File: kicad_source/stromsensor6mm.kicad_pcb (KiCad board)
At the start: 2 copper layers, 47 x 31 mm, 19 parts, among them CN1 SM04B-SRSS-TB, CN10 CONN_01X01, CN11 CONN_01X01, CN2 SM04B-SRSS-TB, CN20 CONN_01X01, CN21 CONN_01X01, CN3 CONN_01X01, U1 INA226

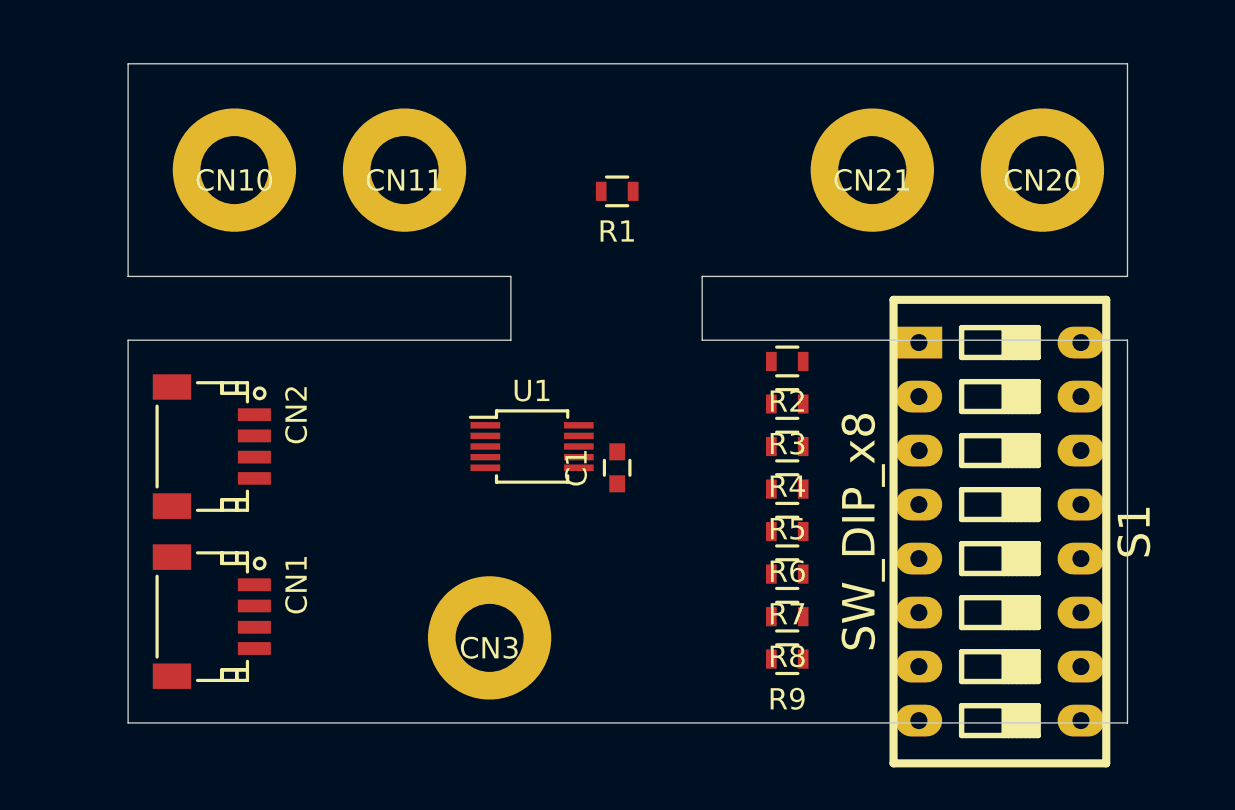
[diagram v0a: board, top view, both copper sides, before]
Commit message: changed mounting holes for connection to wires
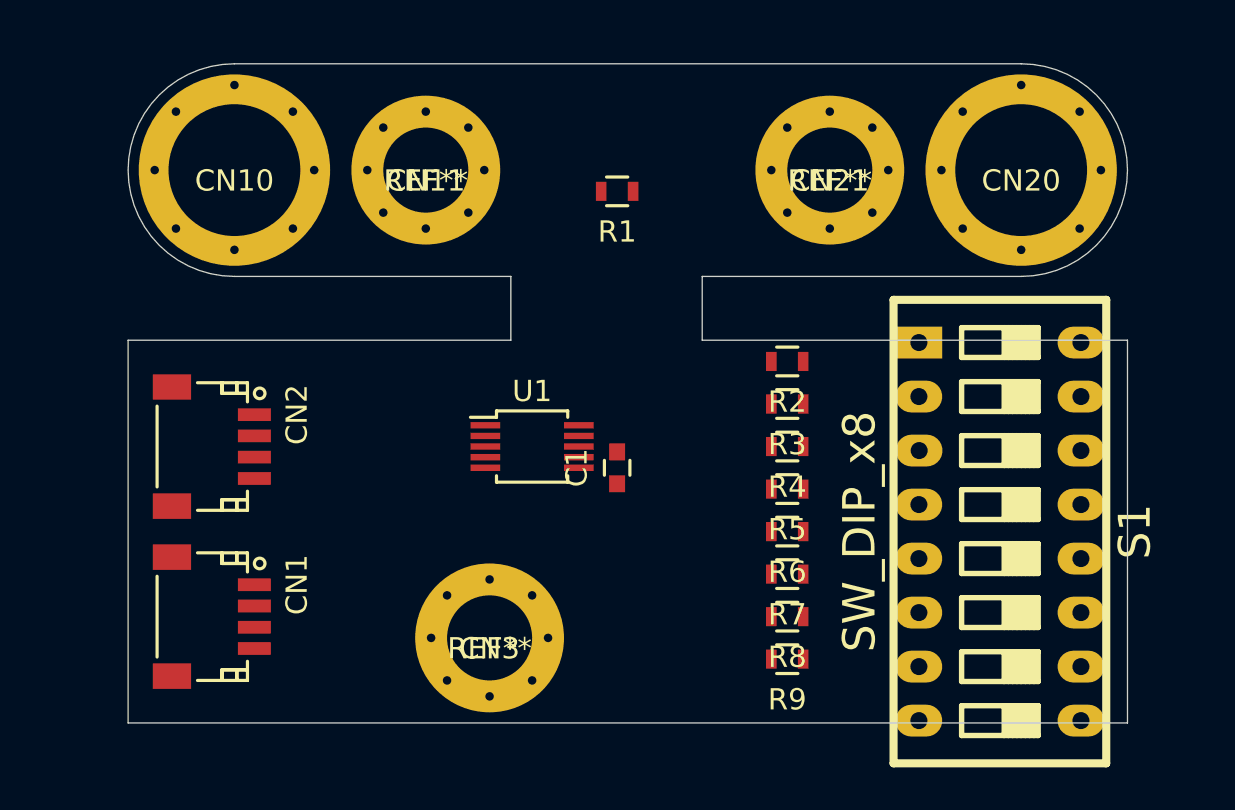
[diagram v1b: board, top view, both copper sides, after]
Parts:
- CN10, CN20: footprint MECH_mounting_holes:MHP_3.2_5.8 -> MECH_mounting_holes:MHP_6.2_9.0
- CN11, CN21, CN3: footprint MECH_mounting_holes:MHP_3.2_5.8 -> MECH_mounting_holes:MHP_4.0_7.0
- moved CN21 2.00 mm to (126.0, 96.0)
- moved CN11 1.00 mm to (107.0, 96.0)
- moved CN20 1.00 mm to (135.0, 96.0)
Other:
- outline, holes or cut-outs redrawn

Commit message: changed current sensor to more robust part
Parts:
- removed R1: 5 mOhm, resistors:R_0603
- added R10: BR3FB5L00, resistors:BR3, F.Cu at (116.0, 97.5)
- added R20: BR3FB5L00, resistors:BR3, F.Cu at (116.0, 94.5)
- moved CN10 4.00 mm to (94.0, 96.0)
- moved CN11 4.00 mm to (103.0, 96.0)
- moved CN20 3.00 mm to (138.0, 96.0)
- moved CN21 3.00 mm to (129.0, 96.0)
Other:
- board size 47 x 31 mm -> 54 x 31 mm

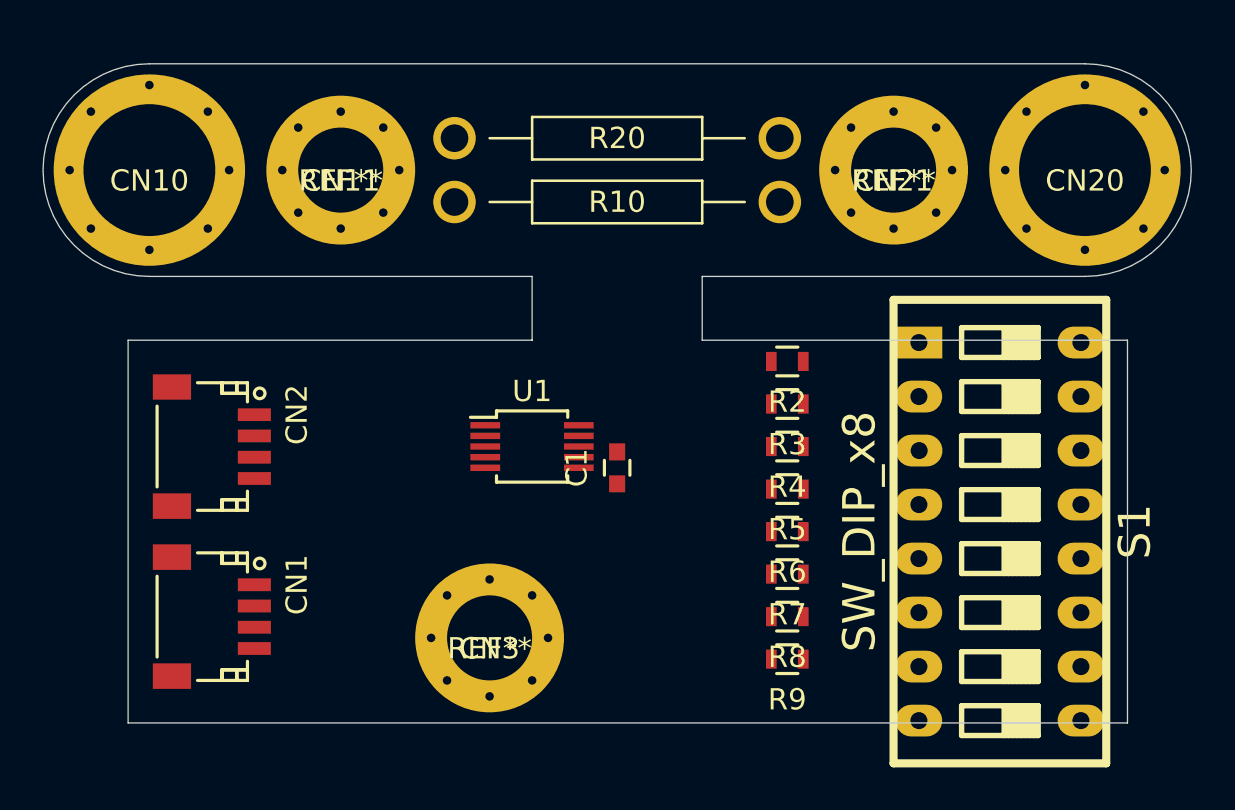
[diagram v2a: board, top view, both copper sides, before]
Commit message: changed dip switch, updated placement and pcb shape
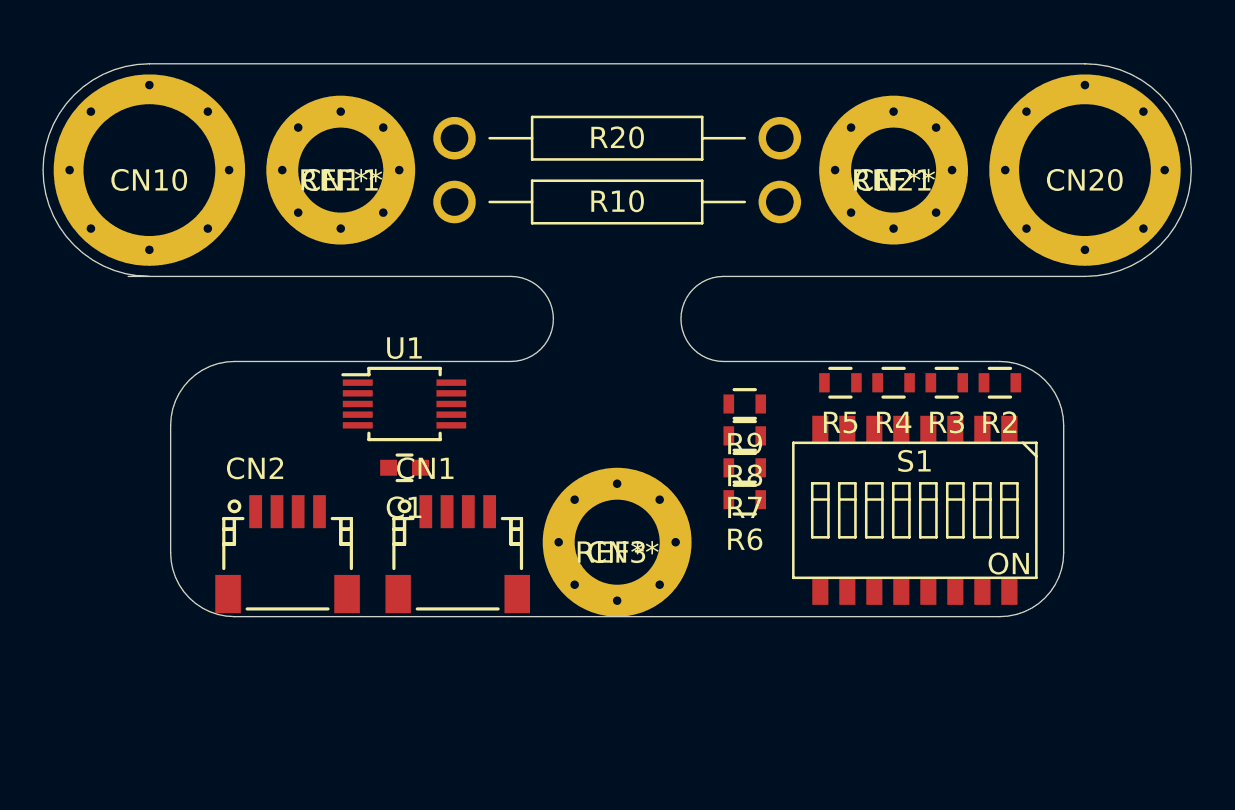
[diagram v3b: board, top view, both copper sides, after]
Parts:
- S1: footprint mechanical-switches:dip_8-300 -> mechanical-switches:WE_416131160808
- moved R9 12.2 mm to (122.0, 107.0)
- moved CN1 11.9 mm to (108.5, 114.0), turned to 0 degrees
- moved R2 10.0 mm to (134.0, 106.0)
- moved C1 10.0 mm to (106.0, 110.0), turned to 180 degrees
- moved R8 8.73 mm to (122.0, 108.5)
- moved R3 7.57 mm to (131.5, 106.0)
- moved CN3 7.50 mm to (116.0, 113.5)
- moved U1 6.32 mm to (106.0, 107.0)
- moved CN2 6.10 mm to (100.5, 114.0), turned to 0 degrees
- moved R4 5.83 mm to (129.0, 106.0)
- moved R5 5.59 mm to (126.5, 106.0)
- moved R7 5.39 mm to (122.0, 110.0)
- moved S1 4.12 mm to (130.0, 112.0), turned to 180 degrees
- moved R6 2.50 mm to (122.0, 111.5)
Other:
- board size 54 x 31 mm -> 54 x 26 mm

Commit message: updated layout, added decoupling capacitor on current sense
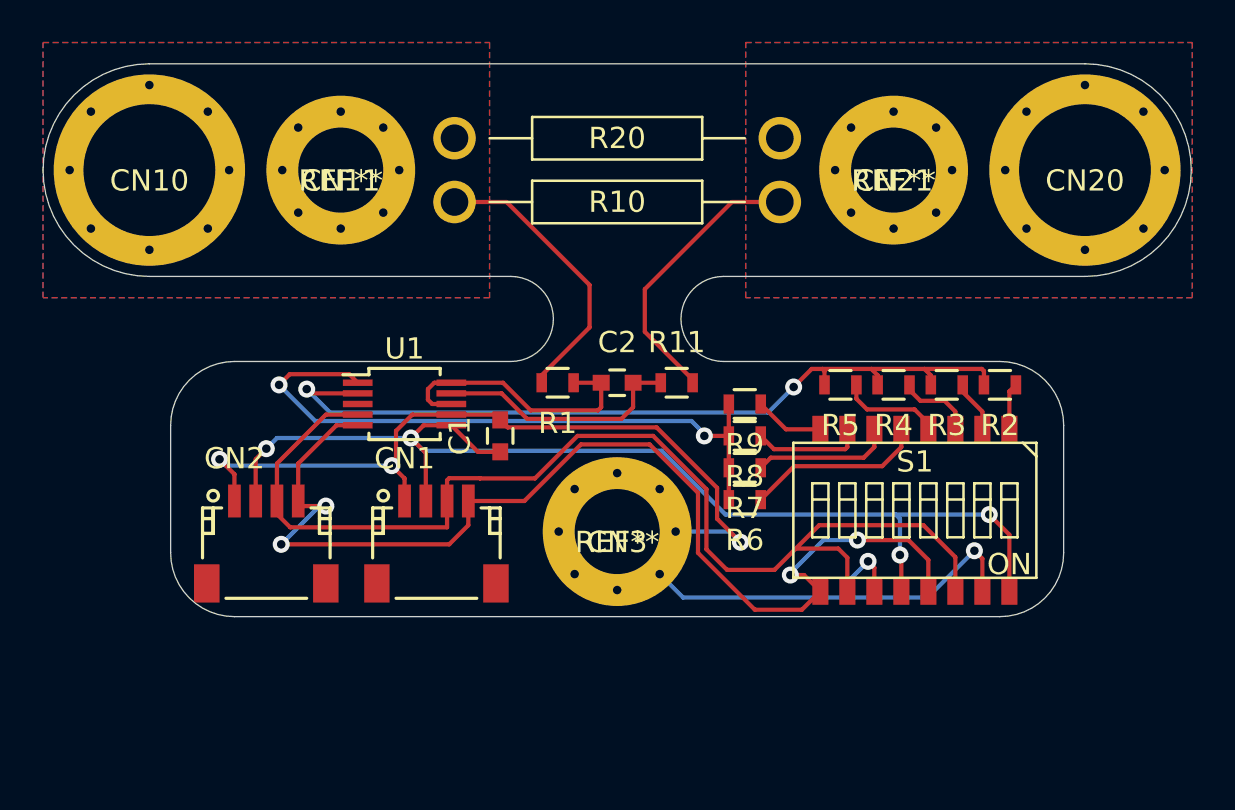
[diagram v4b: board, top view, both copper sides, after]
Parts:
- added C2: 100 nF, capacitors:C_0603, F.Cu at (116.0, 106.0)
- added R1: 100, resistors:R_0603, F.Cu at (113.2, 106.0)
- added R11: 100, resistors:R_0603, F.Cu at (118.8, 106.0)
- moved C1 4.74 mm to (110.5, 108.5), turned to 90 degrees
- moved CN1 1.12 mm to (107.5, 113.5)
- moved CN2 1.12 mm to (99.5, 113.5)
- moved CN3 0.50 mm to (116.0, 113.0)
- moved R2 0.10 mm to (134.0, 106.1)
- moved R3 0.10 mm to (131.5, 106.1)
- moved R4 0.10 mm to (129.0, 106.1)
- moved R5 0.10 mm to (126.5, 106.1)
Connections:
- U1 pad 10: Net-(CN10-Pad1) -> Net-(C2-Pad1)
- U1 pad 8: Net-(CN10-Pad1) -> Net-(C2-Pad1)
- U1 pad 9: Net-(CN20-Pad1) -> Net-(C2-Pad2)
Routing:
- net GND: track 0.00 -> 61.8 mm, vias 0 -> 5
- net +3V3: track 0.00 -> 54.3 mm, vias 0 -> 4
- net /I2C_SDA: track 0.00 -> 53.9 mm
- net /I2C_SCL: track 0.00 -> 53.6 mm, vias 0 -> 4
- net Net-(R2-Pad2): track 0.00 -> 38.9 mm, vias 0 -> 2
- net Net-(R6-Pad2): track 0.00 -> 30.8 mm, vias 0 -> 2
- net Net-(CN10-Pad1): track 0.00 -> 13.5 mm
- net Net-(CN20-Pad1): track 0.00 -> 13.4 mm
- net Net-(C2-Pad1): track 0.00 -> 13.0 mm
- net Net-(C2-Pad2): track 0.00 -> 11.7 mm
- net Net-(R6-Pad1): track 0.00 -> 8.48 mm
- net Net-(R7-Pad1): track 0.00 -> 6.58 mm
- net Net-(R8-Pad1): track 0.00 -> 5.21 mm
- net Net-(R5-Pad1): track 0.00 -> 4.80 mm
- net Net-(R4-Pad1): track 0.00 -> 3.65 mm
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- added copper zone on B.Cu, net Net-(CN10-Pad1)
- added copper zone on F.Cu, net Net-(CN10-Pad1)
- added copper zone on B.Cu, net Net-(CN20-Pad1)
- added copper zone on F.Cu, net Net-(CN20-Pad1)
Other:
- outline, holes or cut-outs redrawn
- net class Default: trace_width 0.25 -> 0.2

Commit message: finished layout
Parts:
- added L1: Label, labels:generationmake_small_silk, F.Cu at (116.1, 102.4)
- added R12: DNI, resistors:R_0603, F.Cu at (98.2, 108.6)
- added R13: DNI, resistors:R_0603, F.Cu at (96.5, 108.6)
- S1: value SW_DIP_x8 -> 218-8LPST
- moved C2 6.05 mm to (110.0, 106.8), turned to 270 degrees
- moved U1 2.21 mm to (103.8, 107.2)
- moved C1 2.20 mm to (108.3, 108.5)
- moved R11 1.30 mm to (117.5, 106.0)
- moved R1 1.20 mm to (114.4, 106.0)
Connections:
- net Net-(C2-Pad1) renamed /IN_R
- net Net-(C2-Pad2) renamed /OUT_R
- net Net-(CN10-Pad1) renamed /IN
- net Net-(CN20-Pad1) renamed /OUT
- net Net-(R2-Pad2) renamed /A0
- net Net-(R6-Pad2) renamed /A1
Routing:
- net /I2C_SCL: track 53.6 -> 59.8 mm
- net GND: track 61.8 -> 66.5 mm, vias 5 -> 12
- net /A0: track 38.9 -> 40.5 mm
- net +3V3: track 54.3 -> 52.8 mm, vias 4 -> 5
- net /I2C_SDA: track 53.9 -> 52.6 mm
- net /IN_R: track 13.0 -> 13.6 mm
- net /OUT: track 13.4 -> 13.9 mm
- net /OUT_R: track 11.7 -> 12.2 mm
- added copper zone on B.Cu, net GND
- added copper zone on F.Cu, net GND
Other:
- board text added: "bot"
- board text added: "stromsensor6mm 0.1"
- board text added: "top"

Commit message: current sensor input filtering works not as intended, changed R1 and R11 to 0 Ohm
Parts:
- R1, R11: value 100 -> 0R

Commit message: added description and documentation in schematic and layout, added pdfs
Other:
- board text added: "Copyright generationmake 2020 see full project documentation at https://github.com/generationmake/Stromsensor6mm This documentation describes Open Hardware and is licensed under the CERN OHL v. 1.2. You may redistribute and modify this documentation under the terms of the CERN OHL v.1.2. (http://ohwr.org/cernohl). This documentation is distributed WITHOUT ANY EXPRESS OR IMPLIED WARRANTY, INCLUDIN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"
